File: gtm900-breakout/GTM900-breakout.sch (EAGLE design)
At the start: 93 parts, among them J1 AUDIO-JACK3, K1 694108106102, T1 BC847, T2 BC847, T3 BC847, T4 BC847, U1 FH12A-40S-0.5SH(55), U3 MCP1827T-ADJE/ET, U4 MIC5366, U5 CP2105-GM, U6 IP4234CZ6, X4 MINI-USB-SHIELD-UX60-MB-5ST

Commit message: gtm900-bo: ERC + DRC done + corrections
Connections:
- removed net N$15: R4.2
- net VIO_2V8: now also R4.2
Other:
- moved on the sheet: TP3, TP4, TP5
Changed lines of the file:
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@@
 <attribute name="LINK" x="83.82" y="27.94" size="1.778" layer="96" rot="R180" display="off"/>
 </instance>
-<instance part="GND9" gate="1" x="88.9" y="20.32"/>
+<instance part="GND9" gate="1" x="88.9" y="17.78"/>
 <instance part="D3" gate="G$1" x="228.6" y="215.9" smashed="yes" rot="R90">
 <attribute name="NAME" x="224.536" y="210.185" size="1.778" layer="95"/>
@@
 <attribute name="TP_SIGNAL_NAME" x="44.45" y="67.31" size="1.778" layer="97"/>
 </instance>
-<instance part="TP3" gate="G$1" x="43.18" y="60.96" smashed="yes">
-<attribute name="DESCRIPTION" x="43.18" y="60.96" size="1.778" layer="96" display="off"/>
-<attribute name="MANUFACTURER" x="43.18" y="60.96" size="1.778" layer="96" display="off"/>
-<attribute name="MANUFACTURERPARTNUMBER" x="43.18" y="60.96" size="1.778" layer="96" display="off"/>
-<attribute name="SOURCE" x="43.18" y="60.96" size="1.778" layer="96" display="off"/>
-<attribute name="SOURCEPARTNUMBER" x="43.18" y="60.96" size="1.778" layer="96" display="off"/>
-<attribute name="ROHSCERTIFICATE" x="43.18" y="60.96" size="1.778" layer="96" display="off"/>
-<attribute name="POPULATED" x="43.18" y="60.96" size="1.778" layer="96" display="off"/>
-<attribute name="CLASS" x="43.18" y="60.96" size="1.778" layer="96" display="off"/>
-<attribute name="LINK" x="43.18" y="60.96" size="1.778" layer="96" display="off"/>
-<attribute name="NAME" x="42.418" y="62.484" size="1.778" layer="95" rot="R180"/>
-<attribute name="TP_SIGNAL_NAME" x="44.45" y="59.69" size="1.778" layer="97"/>
-</instance>
-<instance part="TP4" gate="G$1" x="99.06" y="68.58" smashed="yes">
-<attribute name="DESCRIPTION" x="99.06" y="68.58" size="1.778" layer="96" display="off"/>
-<attribute name="MANUFACTURER" x="99.06" y="68.58" size="1.778" layer="96" display="off"/>
-<attribute name="MANUFACTURERPARTNUMBER" x="99.06" y="68.58" size="1.778" layer="96" display="off"/>
-<attribute name="SOURCE" x="99.06" y="68.58" size="1.778" layer="96" display="off"/>
-<attribute name="SOURCEPARTNUMBER" x="99.06" y="68.58" size="1.778" layer="96" display="off"/>
-<attribute name="ROHSCERTIFICATE" x="99.06" y="68.58" size="1.778" layer="96" display="off"/>
-<attribute name="POPULATED" x="99.06" y="68.58" size="1.778" layer="96" display="off"/>
-<attribute name="CLASS" x="99.06" y="68.58" size="1.778" layer="96" display="off"/>
-<attribute name="LINK" x="99.06" y="68.58" size="1.778" layer="96" display="off"/>
-<attribute name="NAME" x="100.33" y="69.596" size="1.778" layer="95"/>
-<attribute name="TP_SIGNAL_NAME" x="100.33" y="67.31" size="1.778" layer="97"/>
-</instance>
-<instance part="TP5" gate="G$1" x="99.06" y="55.88" smashed="yes" rot="R180">
-<attribute name="DESCRIPTION" x="99.06" y="55.88" size="1.778" layer="96" rot="R180" display="off"/>
-<attribute name="MANUFACTURER" x="99.06" y="55.88" size="1.778" layer="96" rot="R180" display="off"/>
-<attribute name="MANUFACTURERPARTNUMBER" x="99.06" y="55.88" size="1.778" layer="96" rot="R180" display="off"/>
-<attribute name="SOURCE" x="99.06" y="55.88" size="1.778" layer="96" rot="R180" display="off"/>
-<attribute name="SOURCEPARTNUMBER" x="99.06" y="55.88" size="1.778" layer="96" rot="R180" display="off"/>
-<attribute name="ROHSCERTIFICATE" x="99.06" y="55.88" size="1.778" layer="96" rot="R180" display="off"/>
-<attribute name="POPULATED" x="99.06" y="55.88" size="1.778" layer="96" rot="R180" display="off"/>
-<attribute name="CLASS" x="99.06" y="55.88" size="1.778" layer="96" rot="R180" display="off"/>
-<attribute name="LINK" x="99.06" y="55.88" size="1.778" layer="96" rot="R180" display="off"/>
-<attribute name="NAME" x="100.584" y="55.372" size="1.778" layer="95" rot="R180"/>
-<attribute name="TP_SIGNAL_NAME" x="97.79" y="57.15" size="1.778" layer="97" rot="R180"/>
+<instance part="TP3" gate="G$1" x="43.18" y="55.88" smashed="yes" rot="R180">
+<attribute name="DESCRIPTION" x="43.18" y="55.88" size="1.778" layer="96" rot="R180" display="off"/>
+<attribute name="MANUFACTURER" x="43.18" y="55.88" size="1.778" layer="96" rot="R180" display="off"/>
+<attribute name="MANUFACTURERPARTNUMBER" x="43.18" y="55.88" size="1.778" layer="96" rot="R180" display="off"/>
+<attribute name="SOURCE" x="43.18" y="55.88" size="1.778" layer="96" rot="R180" display="off"/>
+<attribute name="SOURCEPARTNUMBER" x="43.18" y="55.88" size="1.778" layer="96" rot="R180" display="off"/>
+<attribute name="ROHSCERTIFICATE" x="43.18" y="55.88" size="1.778" layer="96" rot="R180" display="off"/>
+<attribute name="POPULATED" x="43.18" y="55.88" size="1.778" layer="96" rot="R180" display="off"/>
+<attribute name="CLASS" x="43.18" y="55.88" size="1.778" layer="96" rot="R180" display="off"/>
+<attribute name="LINK" x="43.18" y="55.88" size="1.778" layer="96" rot="R180" display="off"/>
+<attribute name="NAME" x="43.942" y="54.356" size="1.778" layer="95"/>
+<attribute name="TP_SIGNAL_NAME" x="41.91" y="57.15" size="1.778" layer="97" rot="R180"/>
+</instance>
+<instance part="TP4" gate="G$1" x="109.22" y="68.58" smashed="yes">
+<attribute name="DESCRIPTION" x="109.22" y="68.58" size="1.778" layer="96" display="off"/>
+<attribute name="MANUFACTURER" x="109.22" y="68.58" size="1.778" layer="96" display="off"/>
+<attribute name="MANUFACTURERPARTNUMBER" x="109.22" y="68.58" size="1.778" layer="96" display="off"/>
+<attribute name="SOURCE" x="109.22" y="68.58" size="1.778" layer="96" display="off"/>
+<attribute name="SOURCEPARTNUMBER" x="109.22" y="68.58" size="1.778" layer="96" display="off"/>
+<attribute name="ROHSCERTIFICATE" x="109.22" y="68.58" size="1.778" layer="96" display="off"/>
+<attribute name="POPULATED" x="109.22" y="68.58" size="1.778" layer="96" display="off"/>
+<attribute name="CLASS" x="109.22" y="68.58" size="1.778" layer="96" display="off"/>
+<attribute name="LINK" x="109.22" y="68.58" size="1.778" layer="96" display="off"/>
+<attribute name="NAME" x="110.998" y="67.564" size="1.778" layer="95"/>
+<attribute name="TP_SIGNAL_NAME" x="110.49" y="67.31" size="1.778" layer="97"/>
+</instance>
+<instance part="TP5" gate="G$1" x="109.22" y="55.88" smashed="yes" rot="R180">
+<attribute name="DESCRIPTION" x="109.22" y="55.88" size="1.778" layer="96" rot="R180" display="off"/>
+<attribute name="MANUFACTURER" x="109.22" y="55.88" size="1.778" layer="96" rot="R180" display="off"/>
+<attribute name="MANUFACTURERPARTNUMBER" x="109.22" y="55.88" size="1.778" layer="96" rot="R180" display="off"/>
+<attribute name="SOURCE" x="109.22" y="55.88" size="1.778" layer="96" rot="R180" display="off"/>
+<attribute name="SOURCEPARTNUMBER" x="109.22" y="55.88" size="1.778" layer="96" rot="R180" display="off"/>
+<attribute name="ROHSCERTIFICATE" x="109.22" y="55.88" size="1.778" layer="96" rot="R180" display="off"/>
+<attribute name="POPULATED" x="109.22" y="55.88" size="1.778" layer="96" rot="R180" display="off"/>
+<attribute name="CLASS" x="109.22" y="55.88" size="1.778" layer="96" rot="R180" display="off"/>
+<attribute name="LINK" x="109.22" y="55.88" size="1.778" layer="96" rot="R180" display="off"/>
+<attribute name="NAME" x="110.744" y="55.372" size="1.778" layer="95" rot="R180"/>
+<attribute name="TP_SIGNAL_NAME" x="107.95" y="57.15" size="1.778" layer="97" rot="R180"/>
 </instance>
 <instance part="T2" gate="G$1" x="248.92" y="91.44" smashed="yes">
@@
 <pinref part="MDM1" gate="G$1" pin="P$1"/>
 <pinref part="GND9" gate="1" pin="GND"/>
+<wire x1="88.9" y1="20.32" x2="88.9" y2="22.86" width="0.1524" layer="91"/>
 </segment>
 <segment>
@@
 <net name="AUXO-" class="0">
 <segment>
-<wire x1="96.52" y1="66.04" x2="99.06" y2="66.04" width="0.1524" layer="91"/>
-<label x="101.6" y="66.04" size="1.27" layer="95" xref="yes"/>
+<wire x1="96.52" y1="66.04" x2="109.22" y2="66.04" width="0.1524" layer="91"/>
+<label x="111.76" y="66.04" size="1.27" layer="95" xref="yes"/>
 <pinref part="U1" gate="A" pin="7"/>
 <pinref part="TP4" gate="G$1" pin="TP"/>
-<junction x="99.06" y="66.04"/>
-<wire x1="99.06" y1="66.04" x2="101.6" y2="66.04" width="0.1524" layer="91"/>
+<junction x="109.22" y="66.04"/>
+<wire x1="109.22" y1="66.04" x2="111.76" y2="66.04" width="0.1524" layer="91"/>
 </segment>
 </net>
@@
 <segment>
 <pinref part="TP5" gate="G$1" pin="TP"/>
-<wire x1="96.52" y1="58.42" x2="99.06" y2="58.42" width="0.1524" layer="91"/>
-<label x="101.6" y="58.42" size="1.27" layer="95" xref="yes"/>
+<wire x1="96.52" y1="58.42" x2="109.22" y2="58.42" width="0.1524" layer="91"/>
+<label x="111.76" y="58.42" size="1.27" layer="95" xref="yes"/>
 <pinref part="U1" gate="A" pin="1"/>
-<wire x1="99.06" y1="58.42" x2="101.6" y2="58.42" width="0.1524" layer="91"/>
-<junction x="99.06" y="58.42"/>
+<wire x1="109.22" y1="58.42" x2="111.76" y2="58.42" width="0.1524" layer="91"/>
+<junction x="109.22" y="58.42"/>
 </segment>
 </net>
@@
 <label x="251.46" y="114.3" size="1.27" layer="95" rot="R90" xref="yes"/>
 </segment>
+<segment>
+<pinref part="R4" gate="G$1" pin="2"/>
+<wire x1="154.94" y1="213.36" x2="154.94" y2="215.9" width="0.1524" layer="91"/>
+<label x="154.94" y="215.9" size="1.27" layer="95" rot="R90" xref="yes"/>
+</segment>
 </net>
 <net name="N$10" class="0">
@@
 </segment>
 </net>
-<net name="N$15" class="0">
-<segment>
-<pinref part="R4" gate="G$1" pin="2"/>
-<wire x1="154.94" y1="213.36" x2="154.94" y2="215.9" width="0.1524" layer="91"/>
-<label x="154.94" y="215.9" size="1.27" layer="95" rot="R90" xref="yes"/>
-</segment>
-</net>

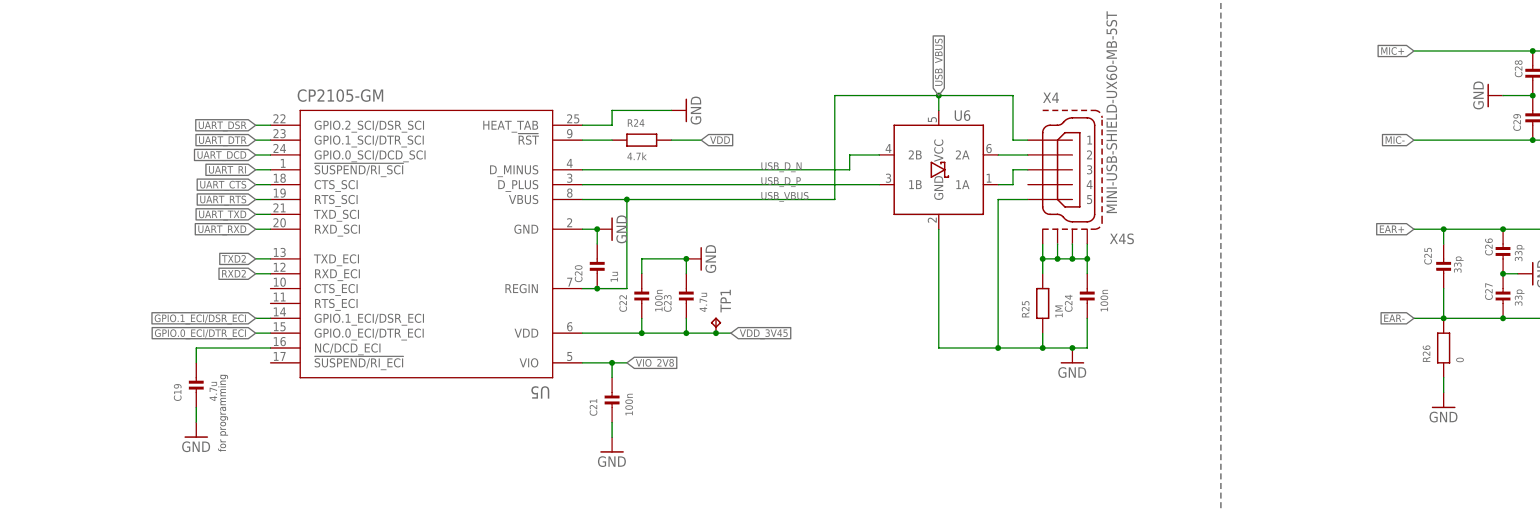
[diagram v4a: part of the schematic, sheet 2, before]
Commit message: gtm900-bo: re-introduce serial 0R on UART_RI
...not, that it was needed, but just in case...
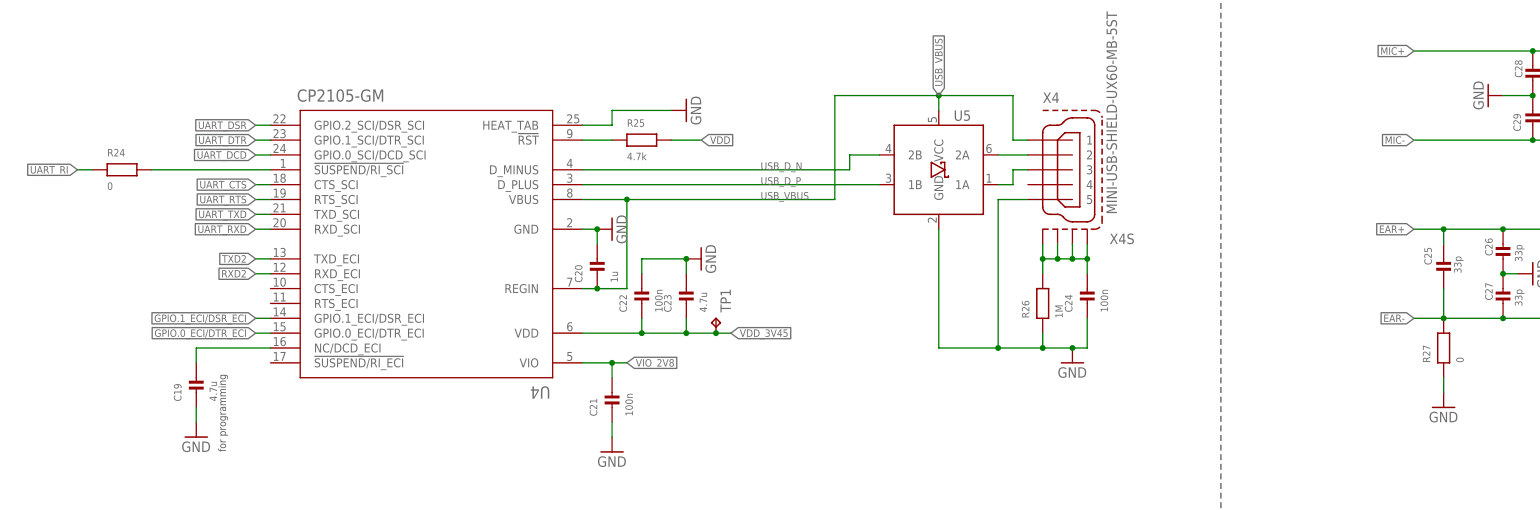
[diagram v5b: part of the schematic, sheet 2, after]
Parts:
- removed U6: IP4234CZ6, laforge:IP4234CZ6
- added R27: 0, rc-sysmocom:RESISTOR_0603
- added U2: MCP1827T-ADJE/ET, ldo:LDO_SHD_ADJMCP1827T-ADJE/ET
- R24: value 4.7k -> 0; DESCRIPTION RES SMD 4.7K OHM 5% 1/10W 0603 -> NO DESCRIPTION; LINK http://www.digikey.com/product-detail/en/yageo/RC0603JR-074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 -> http://www.digikey.de/product-detail/de/AC0402JR-070RL/311-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; MANUFACTURER Yageo -> UNKNOWN MANUFACTURER; MANUFACTURERPARTNUMBER RC0603JR-074K7L -> UNKNOWN MANUFACTURER PART NUMBER; SOURCE DIGIKEY -> UNKNOWN SOURCE; SOURCEPARTNUMBER 311-4.7KGRCT-ND -> UNKNOWN SOURCE PART NUMBER
- R25: value 1M -> 4.7k; DESCRIPTION RES SMD 1M OHM 5% 1/20W 0201 -> RES SMD 4.7K OHM 5% 1/10W 0603; LINK http://www.digikey.com/product-detail/en/samsung-electro-me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 -> http://www.digikey.com/product-detail/en/yageo/RC0603JR-074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; MANUFACTURER Samsung Electro-Mechanics America, Inc. -> Yageo; MANUFACTURERPARTNUMBER RC0603J105CS -> RC0603JR-074K7L; SOURCEPARTNUMBER 1276-3856-1-ND -> 311-4.7KGRCT-ND
- R26: value 0 -> 1M; DESCRIPTION NO DESCRIPTION -> RES SMD 1M OHM 5% 1/20W 0201; LINK http://www.digikey.de/product-detail/de/AC0402JR-070RL/311-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 -> http://www.digikey.com/product-detail/en/samsung-electro-me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; MANUFACTURER UNKNOWN MANUFACTURER -> Samsung Electro-Mechanics America, Inc.; MANUFACTURERPARTNUMBER UNKNOWN MANUFACTURER PART NUMBER -> RC0603J105CS; SOURCE UNKNOWN SOURCE -> DIGIKEY; SOURCEPARTNUMBER UNKNOWN SOURCE PART NUMBER -> 1276-3856-1-ND
- U3: value MCP1827T-ADJE/ET -> MIC5366; device ldo:LDO_SHD_ADJMCP1827T-ADJE/ET -> ldo:LDO_FIXED_EN-MIC5365-YC5; DESCRIPTION Linear Voltage Regulator IC Positive Fixed 1 Output 3.3V 3A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 -> NO DESCRIPTION; LINK http://www.digikey.com/product-detail/en/stmicroelectronics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 -> https://www.digikey.de/product-detail/de/microchip-technolo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; MANUFACTURER STMicroelectronics -> UNKNOWN MANUFACTURER; MANUFACTURERPARTNUMBER LD1085D2T33R -> UNKNOWN MANUFACTURER PART NUMBER; SOURCE DIGIKEY -> UNKNOWN SOURCE; SOURCEPARTNUMBER 497-1222-1-ND -> UNKNOWN SOURCE PART NUMBER
- U4: value MIC5366 -> CP2105-GM; device ldo:LDO_FIXED_EN-MIC5365-YC5 -> usb-uart:CP2105-GM; DESCRIPTION NO DESCRIPTION -> USB Bridge, USB to UART USB 2.0 UART Interface 24-QFN (4x4); LINK https://www.digikey.de/product-detail/de/microchip-technolo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 -> http://www.digikey.com/product-detail/en/silicon-labs/CP210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; MANUFACTURER UNKNOWN MANUFACTURER -> Silicon Labs; MANUFACTURERPARTNUMBER UNKNOWN MANUFACTURER PART NUMBER -> CP2105-F01-GM; SOURCE UNKNOWN SOURCE -> DIGIKEY; SOURCEPARTNUMBER UNKNOWN SOURCE PART NUMBER -> 336-2009-5-ND
- U5: value CP2105-GM -> IP4234CZ6; device usb-uart:CP2105-GM -> laforge:IP4234CZ6; DESCRIPTION USB Bridge, USB to UART USB 2.0 UART Interface 24-QFN (4x4) -> TVS DIODE 5.5VWM 6TSOP; LINK http://www.digikey.com/product-detail/en/silicon-labs/CP210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 -> http://www.digikey.com/product-detail/en/nxp-semiconductors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; MANUFACTURER Silicon Labs -> NXP Semiconductors; MANUFACTURERPARTNUMBER CP2105-F01-GM -> IP4234CZ6,125; SOURCEPARTNUMBER 336-2009-5-ND -> 568-5869-1-ND
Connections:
- new net N$15: R24.2, U4.!SUSPEND/RI_SCI
- net EAR-: now also R27.2; no longer R26.2
- net GND: now also R27.1, U2.GND, U4.HEAT_TAB; no longer R25.1, U5.HEAT_TAB, U6.GND
- net GPIO.0_ECI/DTR_ECI: now also U4.GPIO.0_ECI/DTR_ECI; no longer U5.GPIO.0_ECI/DTR_ECI
- net GPIO.1_ECI/DSR_ECI: now also U4.GPIO.1_ECI/DSR_ECI; no longer U5.GPIO.1_ECI/DSR_ECI
- net LDO_IN: now also U2.!SHDN, U2.IN; no longer U3.!SHDN, U3.IN
- net N$11: now also R26.2; no longer R25.2
- net N$12: now also R25.1, U4.!RST; no longer R24.1, U5.!RST
- net N$14: now also U4.NC/DCD_ECI; no longer U5.NC/DCD_ECI
- net N$6: now also U2.ADJ; no longer U3.ADJ
- net RXD2: now also U4.RXD_ECI; no longer U5.RXD_ECI
- net TXD2: now also U4.TXD_ECI; no longer U5.TXD_ECI
- net UART_CTS: now also U4.CTS_SCI; no longer U5.CTS_SCI
- net UART_DCD: now also U4.GPIO.0_SCI/DCD_SCI; no longer U5.GPIO.0_SCI/DCD_SCI
- net UART_DSR: now also U4.GPIO.2_SCI/DSR_SCI; no longer U5.GPIO.2_SCI/DSR_SCI
- net UART_DTR: now also U4.GPIO.1_SCI/DTR_SCI; no longer U5.GPIO.1_SCI/DTR_SCI
- net UART_RI: now also R24.1; no longer U5.!SUSPEND/RI_SCI
- net UART_RTS: now also U4.RTS_SCI; no longer U5.RTS_SCI
- net UART_RXD: now also U4.RXD_SCI; no longer U5.RXD_SCI
- net UART_TXD: now also U4.TXD_SCI; no longer U5.TXD_SCI
- net USB_D_N: now also U4.D_MINUS, U5.2B; no longer U5.D_MINUS, U6.2B
- net USB_D_P: now also U4.D_PLUS, U5.1B; no longer U5.D_PLUS, U6.1B
- net USB_VBUS: now also U3.EN, U3.IN, U4.REGIN, U4.VBUS, U5.VCC; no longer U4.EN, U4.IN, U5.REGIN, U5.VBUS, U6.VCC
- net VCC: now also U2.OUT; no longer U3.OUT
- net VDD: now also R25.2; no longer R24.2
- net VDD_3V45: now also U4.VDD; no longer U5.VDD
- net VIO_2V8: now also U3.OUT, U4.VIO; no longer U4.OUT, U5.VIO
- net _USB_DN: now also U5.2A; no longer U6.2A
- net _USB_DP: now also U5.1A; no longer U6.1A
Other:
- moved on the sheet: R24, R25, R26

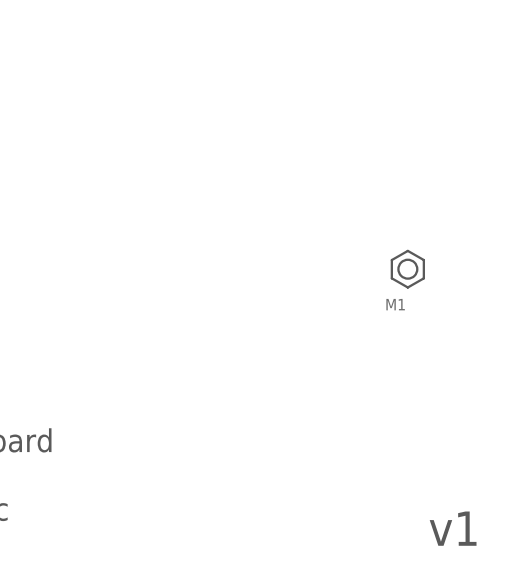
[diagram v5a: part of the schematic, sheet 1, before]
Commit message: gtm900-bo: ease some part's distances, increase OSHW logo
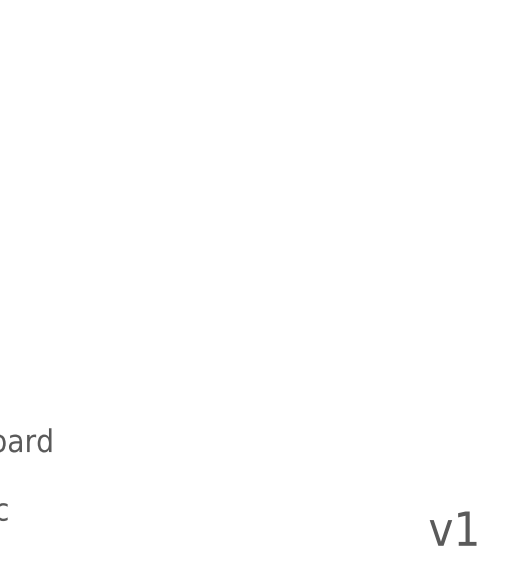
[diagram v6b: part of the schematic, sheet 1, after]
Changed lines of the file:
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@@
 </classes>
 <parts>
-<part name="M1" library="BOM-exclusive" deviceset="NUT" device="">
-<attribute name="LINK" value="http://www.digikey.com/product-detail/en/jae-electronics/MM60-EZH059-B5-R650/670-2277-1-ND"/>
-<attribute name="OC_DIGIKEY" value="H9161CT-ND"/>
-<attribute name="SOURCE" value="DIGIKEY"/>
-<attribute name="SOURCEPARTNUMBER" value="A97593-ND"/>
-</part>
 <part name="SIM1" library="SF7W008S1A-SIM" deviceset="SF7W008S1A" device="-R">
 <attribute name="CLASS" value="UNKNOWN CLASS"/>
@@
 </plain>
 <instances>
-<instance part="M1" gate="G$1" x="373.38" y="35.56">
-<attribute name="OC_DIGIKEY" x="373.38" y="35.56" size="3.81" layer="96" rot="MR0" display="off"/>
-</instance>
 <instance part="SIM1" gate="-CARD" x="96.52" y="208.28">
 <attribute name="DESCRIPTION" x="96.52" y="208.28" size="1.778" layer="96" display="off"/>
